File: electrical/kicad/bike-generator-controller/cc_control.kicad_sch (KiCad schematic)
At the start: 0 parts

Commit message: feat: integrate controller modules and schematics
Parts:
- added J1: J_CC_CTRL, Connector_PinHeader_2.54mm:PinHeader_1x03_P2.54mm_Vertical, symbol Connector_Generic:Conn_01x03
- added R6: 10k, Resistor_SMD:R_0402_1005Metric_Pad0.72x0.64mm_HandSolder, symbol Device:R
- added TP10: CC_W, TestPoint:TestPoint_Pad_D1.5mm, symbol Connector:TestPoint
- added TP11: CC_B, TestPoint:TestPoint_Pad_D1.5mm, symbol Connector:TestPoint
- added TP9: CC_A, TestPoint:TestPoint_Pad_D1.5mm, symbol Connector:TestPoint
- added U3: DFR0520 MCP42100 100k, BikeGenerator:DFR0520_Dual_Digital_Pot, symbol BikeGenerator:DFR0520_Dual_Digital_Pot
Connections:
- new net +3V3: R6.1, U3.6 (VCC)
- new net CC_A: J1.1 (Pin_1), TP9.1, U3.7 (PA0)
- new net CC_B: J1.3 (Pin_3), TP11.1, U3.9 (PB0)
- new net CC_W: J1.2 (Pin_2), TP10.1, U3.8 (PW0)
- new net GND: U3.5 (GND)
- new net POT_CS: R6.2, U3.3 (CS)
- new net POT_MISO: U3.1 (SO)
- new net POT_MOSI: U3.4 (SI)
- new net POT_SCK: U3.2 (SCK)
- no-connect marks 0 -> 3
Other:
- note added: "J1 — 1: PA0 (A) · 2: PW0 (curseur) · 3: PB0 (B)"
- note added: "NE PAS RELIER AU BUCK AVANT MESURES. PA/PW/PB doivent rester entre 0 et 3,3 V et sous ±1 mA par rapport au GND de la carte. POT1 est volontairement inutilisé."

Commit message: feat: establish controller PCB V1 design baseline
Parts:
- removed U3: DFR0520 MCP42100 100k, BikeGenerator:DFR0520_Dual_Digital_Pot, symbol BikeGenerator:DFR0520_Dual_Digital_Pot
- added C12: 100nF X7R, Capacitor_SMD:C_0805_2012Metric_Pad1.18x1.45mm_HandSolder, symbol Device:C
- added U3: MCP4151-104E/SN, Package_SO:SOIC-8_3.9x4.9mm_P1.27mm, symbol Potentiometer_Digital:MCP4151-xxxx-P
- R6: footprint Resistor_SMD:R_0402_1005Metric_Pad0.72x0.64mm_HandSolder -> Resistor_SMD:R_0805_2012Metric_Pad1.20x1.40mm_HandSolder; LCSC (none) -> C84376; MPN (none) -> RC0805FR-0710KL; Manufacturer (none) -> Yageo
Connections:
- net +3V3: now also C12.1, U3.8 (V_{DD})
- net CC_A: now also U3.5 (P0A)
- net CC_B: now also U3.7 (P0B)
- net CC_W: now also U3.6 (P0W)
- net GND: now also C12.2, U3.4 (V_{SS})
- net POT_CS: now also U3.1 (~{CS})
- net POT_MOSI: now also U3.3 (SDI/SDO)
- net POT_SCK: now also U3.2 (SCK)
- no-connect marks 3 -> 0

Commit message: wip: checkpoint controller routing before review
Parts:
- removed TP10: CC_W, TestPoint:TestPoint_Pad_D1.5mm, symbol Connector:TestPoint
- removed TP11: CC_B, TestPoint:TestPoint_Pad_D1.5mm, symbol Connector:TestPoint
- removed TP9: CC_A, TestPoint:TestPoint_Pad_D1.5mm, symbol Connector:TestPoint
- removed U3: MCP4151-104E/SN, Package_SO:SOIC-8_3.9x4.9mm_P1.27mm, symbol Potentiometer_Digital:MCP4151-xxxx-P
- added J9: J_CV_CTRL, Connector_PinHeader_2.54mm:PinHeader_1x03_P2.54mm_Vertical, symbol Connector_Generic:Conn_01x03
- added R19: 10k, Resistor_SMD:R_0805_2012Metric_Pad1.20x1.40mm_HandSolder, symbol Device:R
- added U3: MCP42100-I/SL, Package_SO:SOIC-14_3.9x8.7mm_P1.27mm, symbol Potentiometer_Digital:MCP42100
- renumbered C12 to C4, J1 to J7, R6 to R11
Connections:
- net +3V3: now also C4.2, U3.11 (~{RS}), U3.14 (VDD); no longer C4.1
- net CC_A: now also U3.8 (PA0)
- net CC_B: now also U3.10 (PB0)
- net CC_W: now also U3.9 (PW0)
- net GND: now also C4.1, R19.2, U3.4 (VSS); no longer C4.2
- net POT_CS: now also U3.1 (~{CS})
- net POT_MOSI: now also U3.3 (SI)
- net POT_SCK: now also U3.2 (SCK)
- new net CV_A: J9.1 (Pin_1), U3.7 (PA1)
- new net CV_B: J9.3 (Pin_3), U3.5 (PB1)
- new net CV_W: J9.2 (Pin_2), U3.6 (PW1)
- new net POT_SHDN: R19.1, U3.12 (~{SHDN})
- no-connect marks 0 -> 1
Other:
- note added: "J7 — 1: CC_A (PA0/A) · 2: CC_W (PW0/curseur) · 3: CC_B (PB0/B) J9 — 1: CV_A (PA1/A) · 2: CV_W (PW1/curseur) · 3: CV_B (PB1/B)"
- note added: "NE PAS RELIER J7/J9 AU BUCK AVANT MESURES. A/W/B doivent rester entre 0 et 3,3 V et sous ±1 mA par rapport au GND de la carte."
- note added: "SÉCURITÉ AU DÉMARRAGE : les deux potentiomètres restent en shutdown jusqu’à ce que l’ESP force POT_SHDN à 1."
- note removed: "J1 — 1: PA0 (A) · 2: PW0 (curseur) · 3: PB0 (B)"
- note removed: "NE PAS RELIER AU BUCK AVANT MESURES. PA/PW/PB doivent rester entre 0 et 3,3 V et sous ±1 mA par rapport au GND de la carte. POT1 est volontairement inutilisé."
- moved on the sheet: C4, J7, R11

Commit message: feat: close controller v1 design and define integrated v2
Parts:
- U3: MPN (none) -> MCP42100-I/SL; Manufacturer (none) -> Microchip Technology
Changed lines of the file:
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@@
 			)
 		)
-		(property "Datasheet" "http://ww1.microchip.com/downloads/en/DeviceDoc/11195c.pdf"
+		(property "Datasheet" "https://ww1.microchip.com/downloads/en/devicedoc/11195c.pdf"
 			(at 119.38 90.17 0)
 			(hide yes)
@@
 			(at 119.38 90.17 0)
 			(hide yes)
+			(show_name no)
+			(do_not_autoplace no)
+			(effects
+				(font
+					(size 1.27 1.27)
+				)
+			)
+		)
+		(property "Manufacturer" "Microchip Technology"
+			(at 119.38 90.17 0)
+			(hide yes)
+			(show_name no)
+			(do_not_autoplace no)
+			(effects
+				(font
+					(size 1.27 1.27)
+				)
+			)
+		)
+		(property "MPN" "MCP42100-I/SL"
+			(at 119.38 90.17 0)
+			(hide yes)

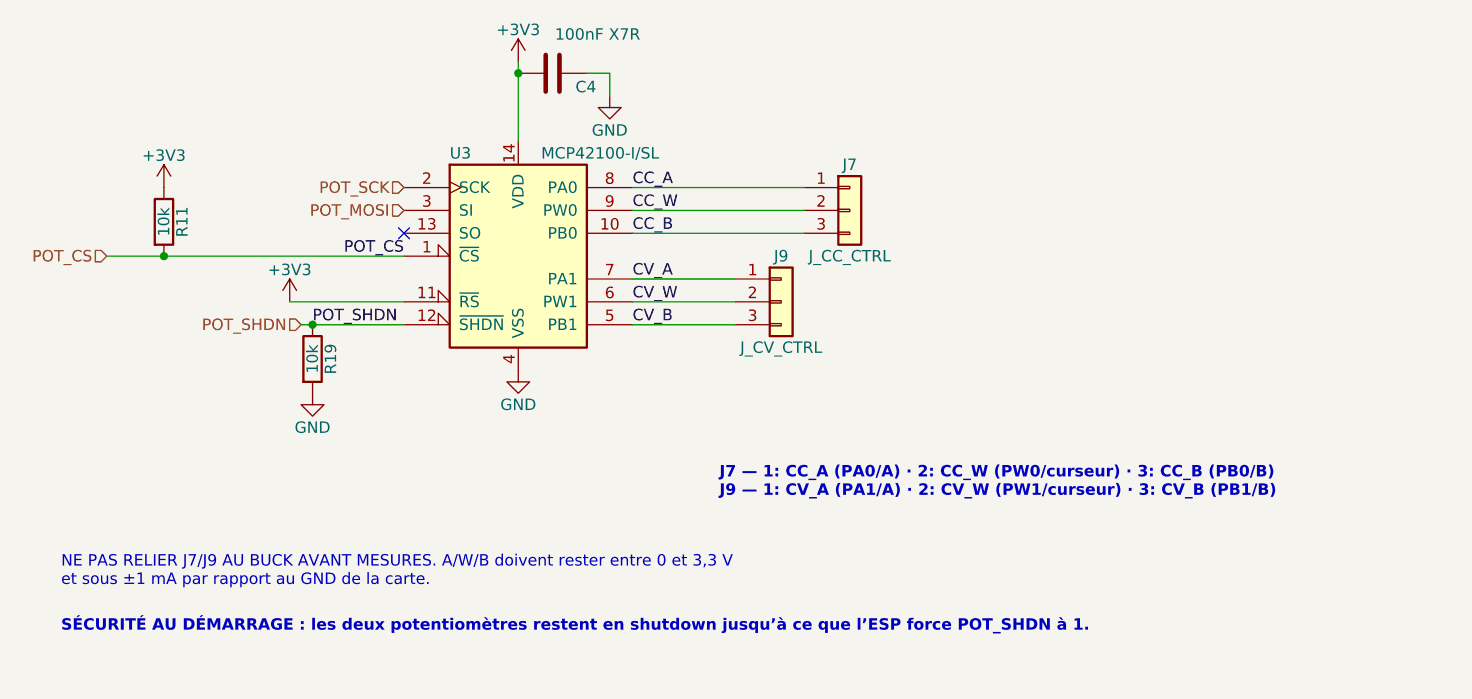
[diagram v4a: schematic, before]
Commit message: feat(controller): finalize V1 design and sourcing
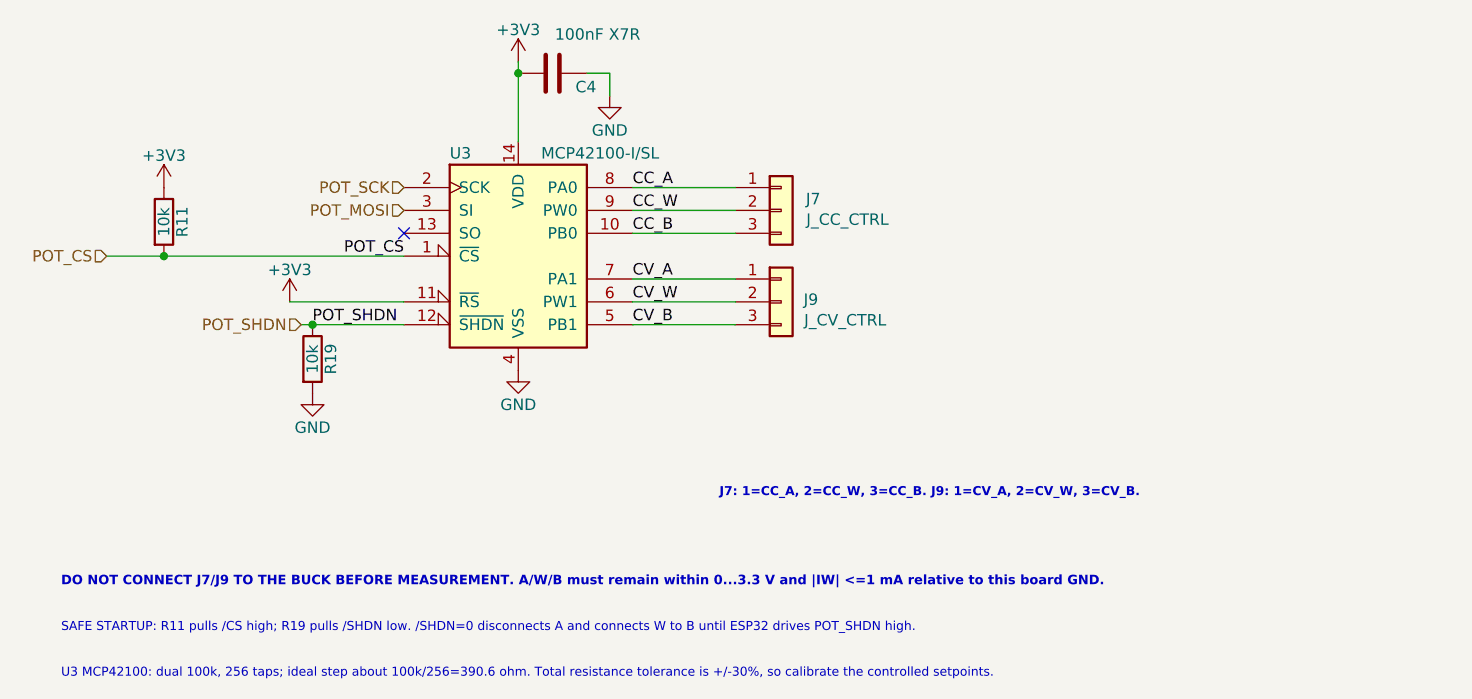
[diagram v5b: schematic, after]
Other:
- note added: "DO NOT CONNECT J7/J9 TO THE BUCK BEFORE MEASUREMENT. A/W/B must remain within 0...3.3 V and |IW| <=1 mA relative to this board GND."
- note added: "J7: 1=CC_A, 2=CC_W, 3=CC_B. J9: 1=CV_A, 2=CV_W, 3=CV_B."
- note added: "SAFE STARTUP: R11 pulls /CS high; R19 pulls /SHDN low. /SHDN=0 disconnects A and connects W to B until ESP32 drives POT_SHDN high."
- note added: "U3 MCP42100: dual 100k, 256 taps; ideal step about 100k/256=390.6 ohm. Total resistance tolerance is +/-30%, so calibrate the controlled setpoints."
- note removed: "J7 — 1: CC_A (PA0/A) · 2: CC_W (PW0/curseur) · 3: CC_B (PB0/B) J9 — 1: CV_A (PA1/A) · 2: CV_W (PW1/curseur) · 3: CV_B (PB1/B)"
- note removed: "NE PAS RELIER J7/J9 AU BUCK AVANT MESURES. A/W/B doivent rester entre 0 et 3,3 V et sous ±1 mA par rapport au GND de la carte."
- note removed: "SÉCURITÉ AU DÉMARRAGE : les deux potentiomètres restent en shutdown jusqu’à ce que l’ESP force POT_SHDN à 1."
- moved on the sheet: J7
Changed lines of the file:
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@@
 	(generator_version "10.0")
 	(paper "A4")
-	(text "NE PAS RELIER J7/J9 AU BUCK AVANT MESURES. A/W/B doivent rester entre 0 et 3,3 V\net sous ±1 mA par rapport au GND de la carte."
+	(text "U3 MCP42100: dual 100k, 256 taps; ideal step about 100k/256=390.6 ohm. Total resistance tolerance is +/-30%, so calibrate the controlled setpoints."
+		(exclude_from_sim no)
+		(at 68.58 137.16 0)
+		(effects
+			(font
+				(size 1 1)
+			)
+			(justify left bottom)
+		)
+	)
+	(text "SAFE STARTUP: R11 pulls /CS high; R19 pulls /SHDN low. /SHDN=0 disconnects A and connects W to B until ESP32 drives POT_SHDN high."
+		(exclude_from_sim no)
+		(at 68.58 132.08 0)
+		(effects
+			(font
+				(size 1 1)
+			)
+			(justify left bottom)
+		)
+	)
+	(text "J7: 1=CC_A, 2=CC_W, 3=CC_B. J9: 1=CV_A, 2=CV_W, 3=CV_B."
+		(exclude_from_sim no)
+		(at 141.732 117.094 0)
+		(effects
+			(font
+				(size 1 1)
+				(bold yes)
+			)
+			(justify left bottom)
+		)
+	)
+	(text "DO NOT CONNECT J7/J9 TO THE BUCK BEFORE MEASUREMENT. A/W/B must remain within 0...3.3 V and |IW| <=1 mA relative to this board GND."
 		(exclude_from_sim no)
 		(at 68.58 127 0)
 		(effects
 			(font
-				(size 1.27 1.27)
-			)
-			(justify left bottom)
-		)
-	)
-	(text "SÉCURITÉ AU DÉMARRAGE : les deux potentiomètres restent en shutdown jusqu’à ce que l’ESP force POT_SHDN à 1."
-		(exclude_from_sim no)
-		(at 68.58 132.08 0)
-		(effects
-			(font
-				(size 1.27 1.27)
-				(bold yes)
-			)
-			(justify left bottom)
-		)
-	)
-	(text "J7 — 1: CC_A (PA0/A) · 2: CC_W (PW0/curseur) · 3: CC_B (PB0/B)\nJ9 — 1: CV_A (PA1/A) · 2: CV_W (PW1/curseur) · 3: CV_B (PB1/B)"
-		(exclude_from_sim no)
-		(at 141.732 117.094 0)
-		(effects
-			(font
-				(size 1.27 1.27)
+				(size 1.05 1.05)
 				(bold yes)
 			)
@@
 	(wire
 		(pts
-			(xy 151.13 85.09) (xy 132.08 85.09)
+			(xy 143.51 85.09) (xy 132.08 85.09)
 		)
 		(stroke
@@
 	(wire
 		(pts
-			(xy 151.13 82.55) (xy 132.08 82.55)
+			(xy 143.51 82.55) (xy 132.08 82.55)
 		)
 		(stroke
@@
 	(wire
 		(pts
-			(xy 151.13 87.63) (xy 132.08 87.63)
+			(xy 143.51 87.63) (xy 132.08 87.63)
 		)
 		(stroke
@@
 	(symbol
 		(lib_id "Connector_Generic:Conn_01x03")
-		(at 156.21 85.09 0)
+		(at 148.59 85.09 0)
 		(unit 1)
 		(body_style 1)
@@
 		(dnp no)
 		(property "Reference" "J7"
-			(at 156.21 80.01 0)
+			(at 152.146 83.82 0)
 			(show_name no)
 			(do_not_autoplace no)
@@
 		)
 		(property "Value" "J_CC_CTRL"
-			(at 156.21 90.17 0)
+			(at 155.956 86.106 0)
 			(show_name no)
 			(do_not_autoplace no)
@@
 		)
 		(property "Footprint" "Connector_PinHeader_2.54mm:PinHeader_1x03_P2.54mm_Vertical"
-			(at 156.21 85.09 0)
+			(at 148.59 85.09 0)
 			(hide yes)
 			(show_name no)
@@
 		)
 		(property "Datasheet" ""
-			(at 156.21 85.09 0)
+			(at 148.59 85.09 0)
 			(hide yes)
 			(show_name no)
@@
 		)
 		(property "Description" "Generic connector, single row, 01x03, script generated (kicad-library-utils/schlib/autogen/connector/)"
-			(at 156.21 85.09 0)
+			(at 148.59 85.09 0)
 			(hide yes)
 			(show_name no)
@@
 		(dnp no)
 		(property "Reference" "J9"
-			(at 148.59 90.17 0)
+			(at 151.892 94.996 0)
 			(show_name no)
 			(do_not_autoplace no)
@@
 		)
 		(property "Value" "J_CV_CTRL"
-			(at 148.59 100.33 0)
-			(show_name no)
-			(do_not_autoplace no)
+			(at 155.702 97.282 0)
+			(show_name no)
+			(do_not_autoplace no)
